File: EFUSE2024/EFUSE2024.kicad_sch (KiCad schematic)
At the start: 1 part

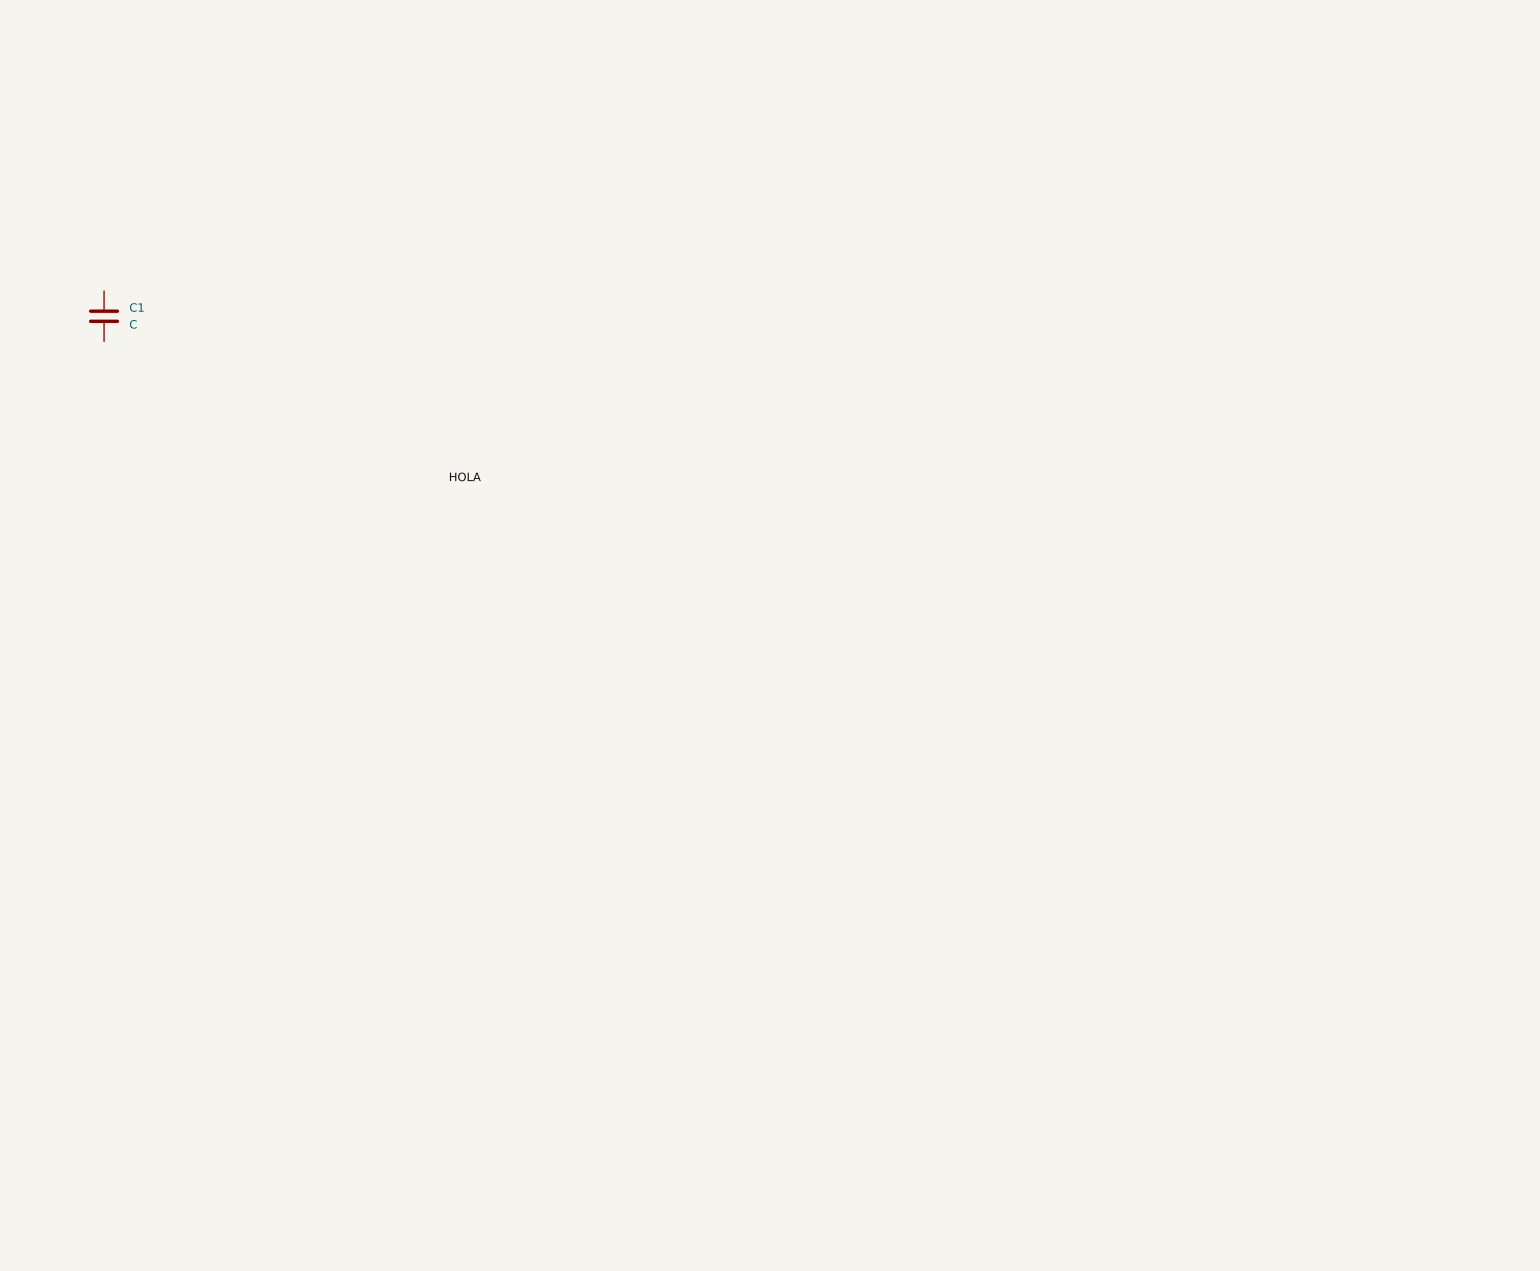
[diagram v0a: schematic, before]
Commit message: added efuses
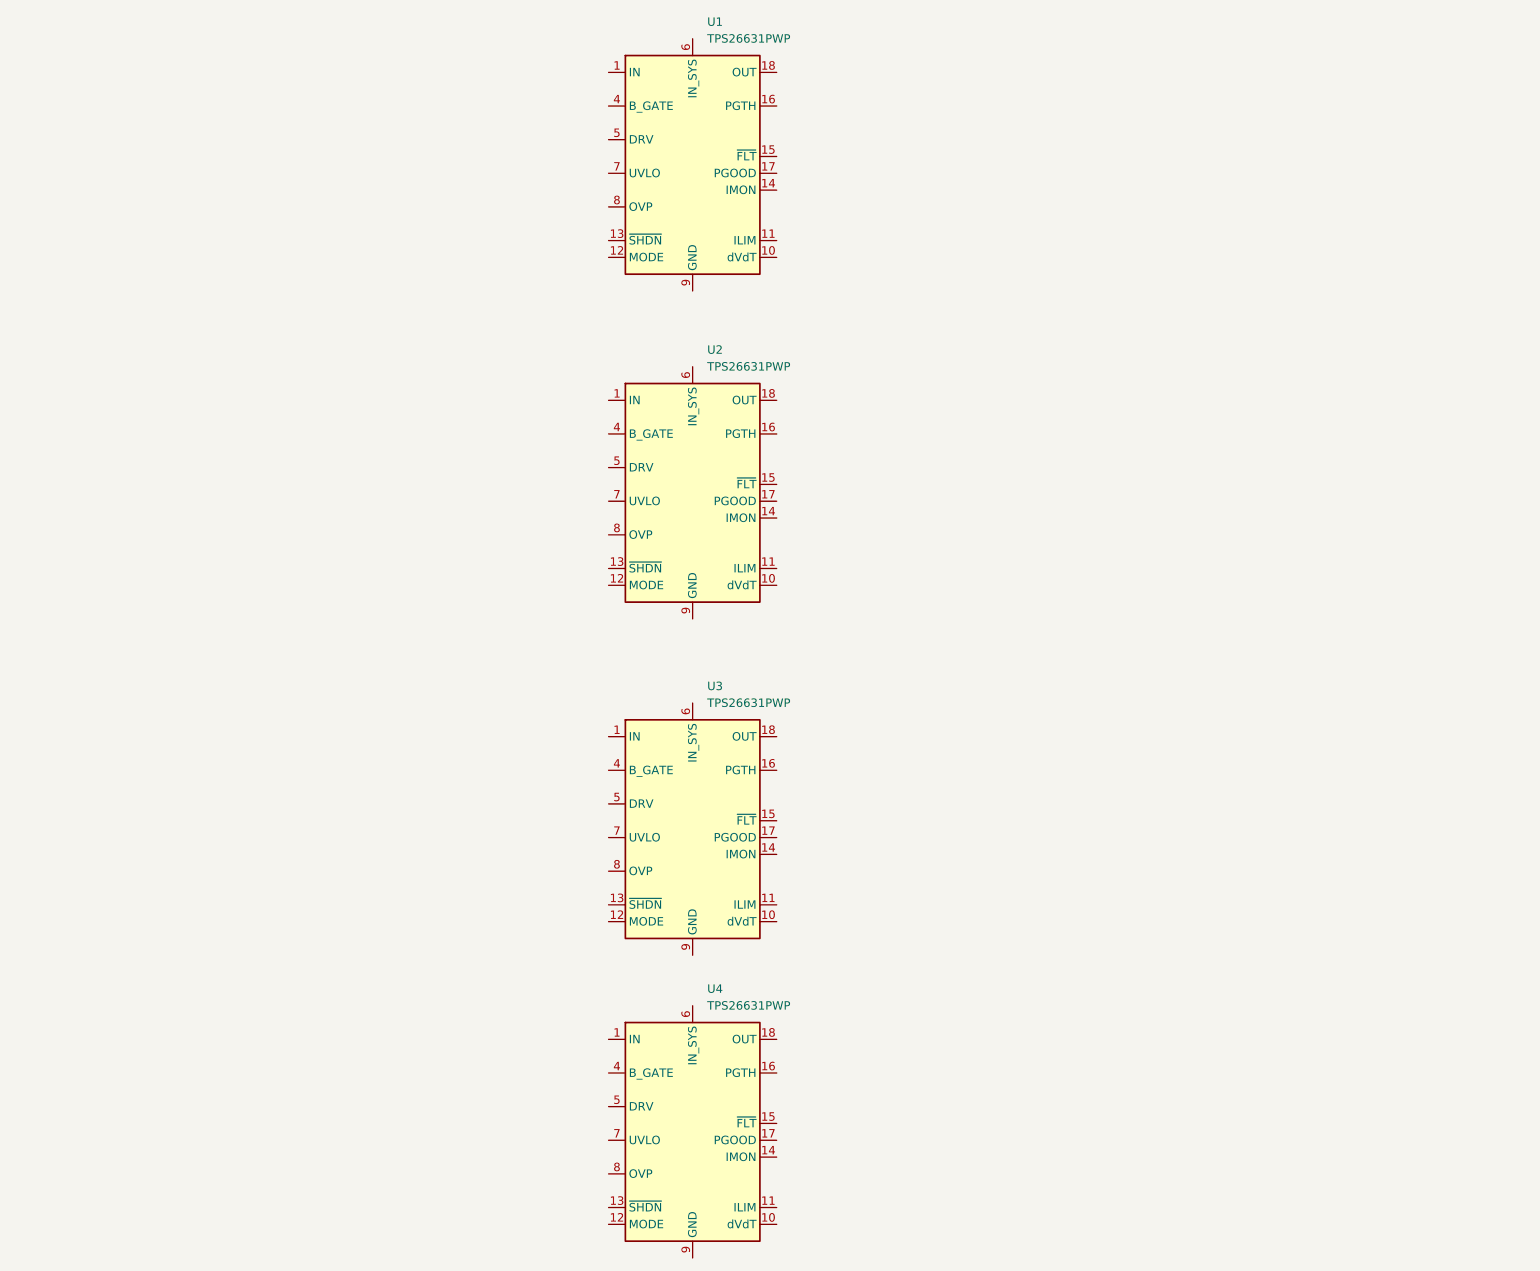
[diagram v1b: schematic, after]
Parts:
- removed C1: C, symbol Device:C
- added U1, U2, U3, U4: TPS26631PWP, Package_SO:HTSSOP-20-1EP_4.4x6.5mm_P0.65mm_EP3.4x6.5mm_Mask2.96x2.96mm_ThermalVias, symbol Power_Management:TPS26631PWP
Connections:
- new net: U1.1 (IN), U1.2 (IN), U1.3 (IN)
- new net: U1.18 (OUT), U1.19 (OUT), U1.20 (OUT)
- new net: U1.21 (GND), U1.9 (GND)
- new net: U3.1 (IN), U3.2 (IN), U3.3 (IN)
- new net: U3.18 (OUT), U3.19 (OUT), U3.20 (OUT)
- new net: U3.21 (GND), U3.9 (GND)
- new net: U2.1 (IN), U2.2 (IN), U2.3 (IN)
- new net: U2.18 (OUT), U2.19 (OUT), U2.20 (OUT)
- new net: U2.21 (GND), U2.9 (GND)
- new net: U4.1 (IN), U4.2 (IN), U4.3 (IN)
- new net: U4.18 (OUT), U4.19 (OUT), U4.20 (OUT)
- new net: U4.21 (GND), U4.9 (GND)

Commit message: Update EFUSE2024.kicad_sch
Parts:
- added C1: C, symbol Device:C
- added Q1, Q2: CSD19532Q5B, Package_TO_SOT_SMD:TDSON-8-1, symbol Transistor_FET:CSD19532Q5B
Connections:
- net at U1.1 (IN), U1.2 (IN), U1.3 (IN): now also Q1.5 (D), Q2.5 (D)
- net at U1.18 (OUT), U1.19 (OUT), U1.20 (OUT): now also Q2.1 (S), Q2.2 (S), Q2.3 (S)
- new net: C1.1, Q1.1 (S), Q1.2 (S), Q1.3 (S)

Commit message: Update EFUSE2024.kicad_sch
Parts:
- C1: value C -> 0.1uF
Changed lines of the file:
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@@
 			)
 		)
-		(property "Value" "C"
+		(property "Value" "0.1uF"
 			(at 110.49 27.9399 0)
 			(effects

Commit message: test
something
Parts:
- added C2, C3, C4, C5, C6, C7, C8: 0.1uF, symbol Device:C
- added D1: 1.5SMCxxCA, Diode_SMD:D_SMC, symbol Diode:1.5SMCxxCA
- added Q3, Q4, Q6: CSD19532Q5B, Package_TO_SOT_SMD:TDSON-8-1, symbol Transistor_FET:CSD19532Q5B
- added Q7: BSS138, Package_TO_SOT_SMD:SOT-23, symbol Transistor_FET:BSS138
- added R1, R2, R3, R4, R5, R6, R7, R8: R, symbol Device:R
- added U5, U6: TPS26631PWP, Package_SO:HTSSOP-20-1EP_4.4x6.5mm_P0.65mm_EP3.4x6.5mm_Mask2.96x2.96mm_ThermalVias, symbol Power_Management:TPS26631PWP
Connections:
- new net: R2.2, R3.1, U5.8 (OVP), U6.8 (OVP)
- new net: C2.1, C4.1, D1.2 (A2), Q3.1 (S), Q3.2 (S), Q3.3 (S), Q7.3 (D), R1.1, U5.6 (IN_SYS)
- new net: R6.1, U5.11 (ILIM)
- new net: C8.1, Q3.5 (D), Q4.5 (D), Q6.5 (D), U5.1 (IN), U5.2 (IN), U5.3 (IN), U6.1 (IN), U6.2 (IN), U6.3 (IN), U6.6 (IN_SYS)
- new net: C3.1, C5.1, C7.1, Q4.1 (S), Q4.2 (S), Q4.3 (S), Q6.1 (S), Q6.2 (S), Q6.3 (S), R4.1, U5.18 (OUT), U5.19 (OUT), U5.20 (OUT), U6.18 (OUT), U6.19 (OUT), U6.20 (OUT)
- new net: R4.2, R5.1, U5.16 (PGTH)
- new net: C6.1, U5.10 (dVdT), U6.10 (dVdT)
- new net: R8.1, U6.11 (ILIM)
- new net: U5.13 (~{SHDN}), U6.13 (~{SHDN})
- new net: R7.1, U5.14 (IMON), U6.14 (IMON)
- new net: R1.2, R2.1, U5.7 (UVLO), U6.7 (UVLO)
- new net: Q3.4 (G), Q7.2 (S), U5.4 (B_GATE)
- new net: Q7.1 (G), U5.5 (DRV)
- new net GND: C2.2, C3.2, C4.2, C5.2, C6.2, C7.2, C8.2, D1.1 (A1), R3.2, R5.2, R6.2, R7.2, R8.2, U5.12 (MODE), U5.21 (GND), U5.9 (GND), U6.12 (MODE), U6.21 (GND), U6.9 (GND)
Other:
- moved on the sheet: C1, Q1, Q2, U1, U2, U3, U4

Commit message: For Nitya
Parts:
- removed C1: 0.1uF, symbol Device:C
- removed Q1, Q2, Q6: CSD19532Q5B, Package_TO_SOT_SMD:TDSON-8-1, symbol Transistor_FET:CSD19532Q5B
- removed U1, U2, U3, U4: TPS26631PWP, Package_SO:HTSSOP-20-1EP_4.4x6.5mm_P0.65mm_EP3.4x6.5mm_Mask2.96x2.96mm_ThermalVias, symbol Power_Management:TPS26631PWP
- added U7: TPS26630RGE, Package_DFN_QFN:Texas_RGE0024H_VQFN-24-1EP_4x4mm_P0.5mm_EP2.7x2.7mm_ThermalVias, symbol Power_Management:TPS26630RGE
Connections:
- new net: U7.1 (IN), U7.2 (IN)
- new net: U7.17 (OUT), U7.18 (OUT)
- new net: U7.25 (GND), U7.8 (GND)
